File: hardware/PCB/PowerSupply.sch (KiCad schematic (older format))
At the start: 14 parts

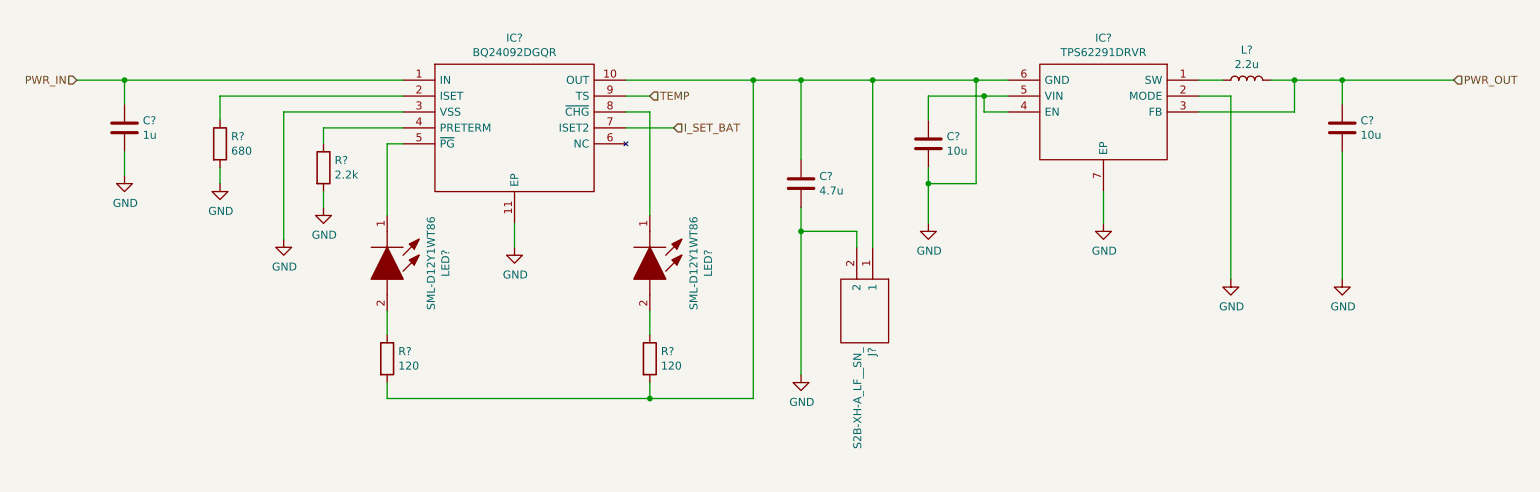
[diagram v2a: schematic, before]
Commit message: complete display circuit
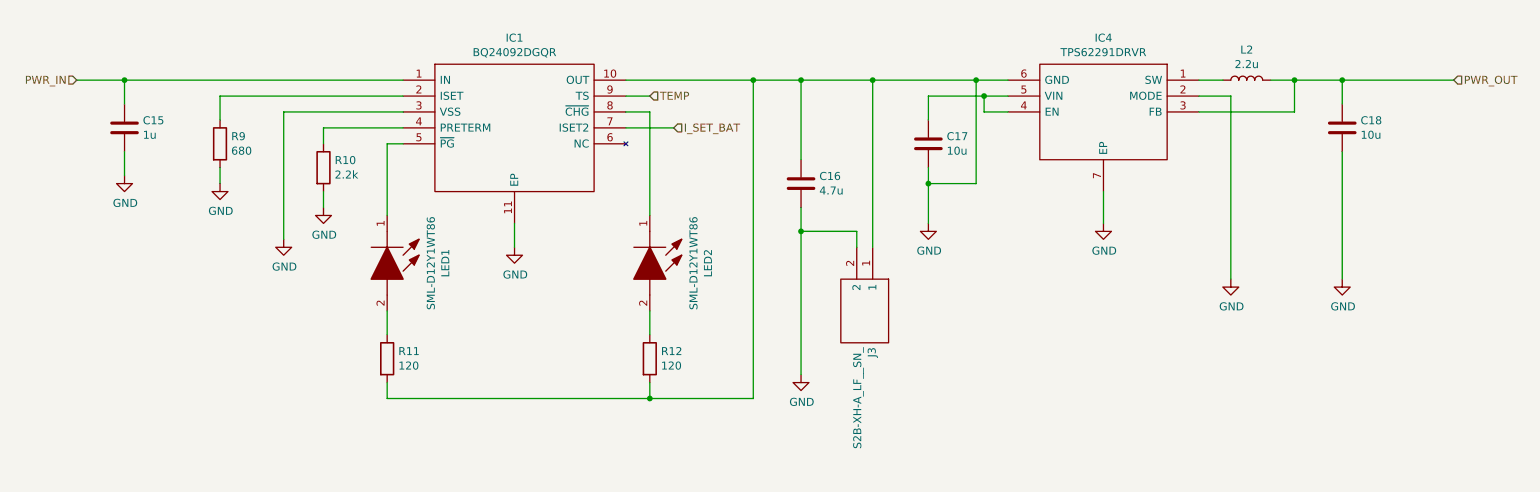
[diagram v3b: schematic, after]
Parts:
- gave numbers to parts that had none: 14
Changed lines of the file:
@@
 $EndDescr
 $Comp
-L ProjectLibrary:BQ24092DGQR IC?
+L ProjectLibrary:BQ24092DGQR IC1
 U 1 1 5FC01F89
 P 3250 1350
-F 0 "IC?" H 3950 1615 50  0000 C CNN
+F 0 "IC1" H 3950 1615 50  0000 C CNN
 F 1 "BQ24092DGQR" H 3950 1524 50  0000 C CNN
 F 2 "SOP50P490X110-11N" H 4500 1450 50  0001 L CNN
@@
 $EndComp
 $Comp
-L Device:C C?
+L Device:C C15
 U 1 1 5FC0418B
 P 1500 1650
-F 0 "C?" H 1615 1696 50  0000 L CNN
+F 0 "C15" H 1615 1696 50  0000 L CNN
 F 1 "1u" H 1615 1605 50  0000 L CNN
 F 2 "Capacitor_SMD:C_0603_1608Metric" H 1538 1500 50  0001 C CNN
@@
 Connection ~ 1500 1350
 $Comp
-L power:GND #PWR?
+L power:GND #PWR024
 U 1 1 5FC0983B
 P 2500 2350
-F 0 "#PWR?" H 2500 2100 50  0001 C CNN
+F 0 "#PWR024" H 2500 2100 50  0001 C CNN
 F 1 "GND" H 2505 2177 50  0000 C CNN
 F 2 "" H 2500 2350 50  0001 C CNN
@@
 	2500 1550 2500 2350
 $Comp
-L power:GND #PWR?
+L power:GND #PWR022
 U 1 1 5FC0A0A3
 P 1500 1950
-F 0 "#PWR?" H 1500 1700 50  0001 C CNN
+F 0 "#PWR022" H 1500 1700 50  0001 C CNN
 F 1 "GND" H 1505 1777 50  0000 C CNN
 F 2 "" H 1500 1950 50  0001 C CNN
@@
 $EndComp
 $Comp
-L Device:R R?
+L Device:R R9
 U 1 1 5FC0ABBE
 P 2100 1750
-F 0 "R?" H 2170 1796 50  0000 L CNN
+F 0 "R9" H 2170 1796 50  0000 L CNN
 F 1 "680" H 2170 1705 50  0000 L CNN
 F 2 "Resistor_SMD:R_0603_1608Metric" V 2030 1750 50  0001 C CNN
@@
 	2100 1900 2100 2000
 $Comp
-L power:GND #PWR?
+L power:GND #PWR023
 U 1 1 5FC0FEEE
 P 2100 2000
-F 0 "#PWR?" H 2100 1750 50  0001 C CNN
+F 0 "#PWR023" H 2100 1750 50  0001 C CNN
 F 1 "GND" H 2105 1827 50  0000 C CNN
 F 2 "" H 2100 2000 50  0001 C CNN
@@
 	2500 1550 3250 1550
 $Comp
-L Device:R R?
+L Device:R R10
 U 1 1 5FC11D4B
 P 2750 1900
-F 0 "R?" H 2820 1946 50  0000 L CNN
+F 0 "R10" H 2820 1946 50  0000 L CNN
 F 1 "2.2k" H 2820 1855 50  0000 L CNN
 F 2 "Resistor_SMD:R_0603_1608Metric" V 2680 1900 50  0001 C CNN
@@
 	2750 2050 2750 2150
 $Comp
-L power:GND #PWR?
+L power:GND #PWR025
 U 1 1 5FC12359
 P 2750 2150
-F 0 "#PWR?" H 2750 1900 50  0001 C CNN
+F 0 "#PWR025" H 2750 1900 50  0001 C CNN
 F 1 "GND" H 2755 1977 50  0000 C CNN
 F 2 "" H 2750 2150 50  0001 C CNN
@@
 $EndComp
 $Comp
-L power:GND #PWR?
+L power:GND #PWR026
 U 1 1 5FC12BAC
 P 3950 2400
-F 0 "#PWR?" H 3950 2150 50  0001 C CNN
+F 0 "#PWR026" H 3950 2150 50  0001 C CNN
 F 1 "GND" H 3955 2227 50  0000 C CNN
 F 2 "" H 3950 2400 50  0001 C CNN
@@
 PWR_OUT
 $Comp
-L ProjectLibrary:SML-D12Y1WT86 LED?
+L ProjectLibrary:SML-D12Y1WT86 LED1
 U 1 1 5FC1DAA7
 P 3150 2200
-F 0 "LED?" H 3450 2567 50  0000 C CNN
+F 0 "LED1" H 3450 2567 50  0000 C CNN
 F 1 "SML-D12Y1WT86" H 3450 2476 50  0000 C CNN
 F 2 "LEDC1608X55N" H 3650 2350 50  0001 L BNN
@@
 $EndComp
 $Comp
-L ProjectLibrary:SML-D12Y1WT86 LED?
+L ProjectLibrary:SML-D12Y1WT86 LED2
 U 1 1 5FC2377E
 P 4800 2200
-F 0 "LED?" H 5100 2567 50  0000 C CNN
+F 0 "LED2" H 5100 2567 50  0000 C CNN
 F 1 "SML-D12Y1WT86" H 5100 2476 50  0000 C CNN
 F 2 "LEDC1608X55N" H 5300 2350 50  0001 L BNN
@@
 	3150 2200 3150 1750
 $Comp
-L Device:R R?
+L Device:R R11
 U 1 1 5FC29AD8
 P 3150 3100
-F 0 "R?" H 3220 3146 50  0000 L CNN
+F 0 "R11" H 3220 3146 50  0000 L CNN
 F 1 "120" H 3220 3055 50  0000 L CNN
 F 2 "Resistor_SMD:R_0603_1608Metric" V 3080 3100 50  0001 C CNN
@@
 $EndComp
 $Comp
-L Device:R R?
+L Device:R R12
 U 1 1 5FC2A161
 P 4800 3100
-F 0 "R?" H 4870 3146 50  0000 L CNN
+F 0 "R12" H 4870 3146 50  0000 L CNN
 F 1 "120" H 4870 3055 50  0000 L CNN
 F 2 "Resistor_SMD:R_0603_1608Metric" V 4730 3100 50  0001 C CNN
@@
 	3950 2250 3950 2400
 $Comp
-L Device:C C?
+L Device:C C16
 U 1 1 5FC2DE09
 P 5750 2000
-F 0 "C?" H 5865 2046 50  0000 L CNN
+F 0 "C16" H 5865 2046 50  0000 L CNN
 F 1 "4.7u" H 5865 1955 50  0000 L CNN
 F 2 "Capacitor_SMD:C_0603_1608Metric" H 5788 1850 50  0001 C CNN
@@
 $EndComp
 $Comp
-L power:GND #PWR?
+L power:GND #PWR027
 U 1 1 5FC2E9CD
 P 5750 3200
-F 0 "#PWR?" H 5750 2950 50  0001 C CNN
+F 0 "#PWR027" H 5750 2950 50  0001 C CNN
 F 1 "GND" H 5755 3027 50  0000 C CNN
 F 2 "" H 5750 3200 50  0001 C CNN
@@
 	5750 1350 6200 1350
 $Comp
-L ProjectLibrary:S2B-XH-A_LF__SN_ J?
+L ProjectLibrary:S2B-XH-A_LF__SN_ J3
 U 1 1 5FC2F7E2
 P 6200 2400
-F 0 "J?" H 6828 2396 50  0000 L CNN
+F 0 "J3" H 6828 2396 50  0000 L CNN
 F 1 "S2B-XH-A_LF__SN_" H 6828 2305 50  0000 L CNN
 F 2 "SHDRRA2W80P0X250_1X2_740X1150X610P" H 6850 2500 50  0001 L CNN
@@
 $EndComp
 $Comp
-L ProjectLibrary:TPS62291DRVR IC?
+L ProjectLibrary:TPS62291DRVR IC4
 U 1 1 5FC09EEE
 P 8250 1350
-F 0 "IC?" H 8850 1615 50  0000 C CNN
+F 0 "IC4" H 8850 1615 50  0000 C CNN
 F 1 "TPS62291DRVR" H 8850 1524 50  0000 C CNN
 F 2 "SON65P200X200X80-7N" H 9300 1450 50  0001 L CNN
@@
 $EndComp
 $Comp
-L power:GND #PWR?
+L power:GND #PWR028
 U 1 1 5FC12B1D
 P 6550 2250
-F 0 "#PWR?" H 6550 2000 50  0001 C CNN
+F 0 "#PWR028" H 6550 2000 50  0001 C CNN
 F 1 "GND" H 6555 2077 50  0000 C CNN
 F 2 "" H 6550 2250 50  0001 C CNN
@@
 $EndComp
 $Comp
-L Device:C C?
+L Device:C C17
 U 1 1 5FC139FA
 P 6550 1750
-F 0 "C?" H 6665 1796 50  0000 L CNN
+F 0 "C17" H 6665 1796 50  0000 L CNN
 F 1 "10u" H 6665 1705 50  0000 L CNN
 F 2 "" H 6588 1600 50  0001 C CNN
@@
 	8250 1450 8450 1450
 $Comp
-L power:GND #PWR?
+L power:GND #PWR030
 U 1 1 5FC1A4A2
 P 8450 2600
-F 0 "#PWR?" H 8450 2350 50  0001 C CNN
+F 0 "#PWR030" H 8450 2350 50  0001 C CNN
 F 1 "GND" H 8455 2427 50  0000 C CNN
 F 2 "" H 8450 2600 50  0001 C CNN
@@
 $EndComp
 $Comp
-L power:GND #PWR?
+L power:GND #PWR029
 U 1 1 5FC1D2CA
 P 7650 2250
-F 0 "#PWR?" H 7650 2000 50  0001 C CNN
+F 0 "#PWR029" H 7650 2000 50  0001 C CNN
 F 1 "GND" H 7655 2077 50  0000 C CNN
 F 2 "" H 7650 2250 50  0001 C CNN
@@
 	7650 2050 7650 2250
 $Comp
-L Device:L L?
+L Device:L L2
 U 1 1 5FC1EB27
 P 8550 1350
-F 0 "L?" V 8740 1350 50  0000 C CNN
+F 0 "L2" V 8740 1350 50  0000 C CNN
 F 1 "2.2u" V 8649 1350 50  0000 C CNN
 F 2 "" H 8550 1350 50  0001 C CNN
@@
 	8250 1350 8400 1350
 $Comp
-L Device:C C?
+L Device:C C18
 U 1 1 5FC33F95
 P 9150 1650
-F 0 "C?" H 9265 1696 50  0000 L CNN
+F 0 "C18" H 9265 1696 50  0000 L CNN
 F 1 "10u" H 9265 1605 50  0000 L CNN
 F 2 "" H 9188 1500 50  0001 C CNN
@@
 	9150 1500 9150 1350
 $Comp
-L power:GND #PWR?
+L power:GND #PWR031
 U 1 1 5FC4D9AD
 P 9150 2600
-F 0 "#PWR?" H 9150 2350 50  0001 C CNN
+F 0 "#PWR031" H 9150 2350 50  0001 C CNN
 F 1 "GND" H 9155 2427 50  0000 C CNN
 F 2 "" H 9150 2600 50  0001 C CNN

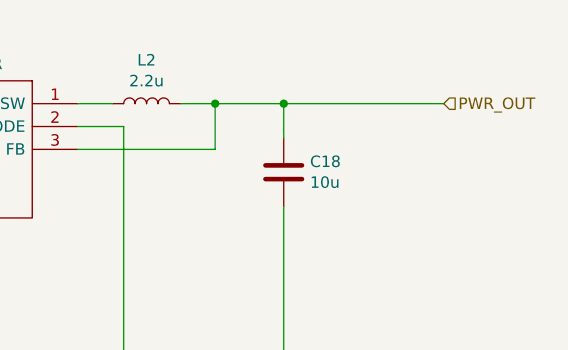
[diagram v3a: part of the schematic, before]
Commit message: change power out to 3V3
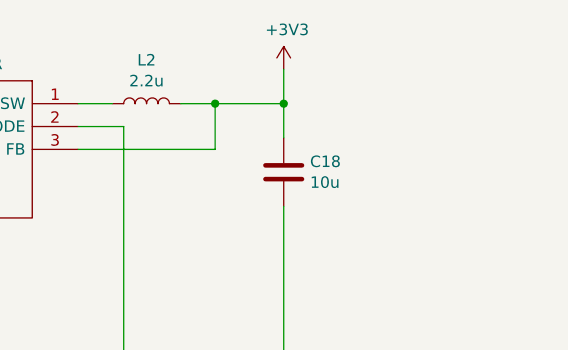
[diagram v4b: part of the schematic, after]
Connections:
- net PWR_OUT renamed +3V3
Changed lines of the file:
@@
 $Descr A4 11693 8268
 encoding utf-8
-Sheet 3 3
+Sheet 2 3
 Title ""
 Date ""
@@
 Wire Wire Line
 	4650 1550 4800 1550
-Text HLabel 9850 1350 2    50   Input ~ 0
-PWR_OUT
 $Comp
 L ProjectLibrary:SML-D12Y1WT86 LED1
@@
 	8850 1350 9150 1350
 Connection ~ 9150 1350
-Wire Wire Line
-	9150 1350 9850 1350
+$Comp
+L power:+3V3 #PWR?
+U 1 1 5FCF0BC9
+P 9150 1200
+F 0 "#PWR?" H 9150 1050 50  0001 C CNN
+F 1 "+3V3" H 9165 1373 50  0000 C CNN
+F 2 "" H 9150 1200 50  0001 C CNN
+F 3 "" H 9150 1200 50  0001 C CNN
+	1    9150 1200
+	1    0    0    -1
+$EndComp
+Wire Wire Line
+	9150 1200 9150 1350
 $EndSCHEMATC

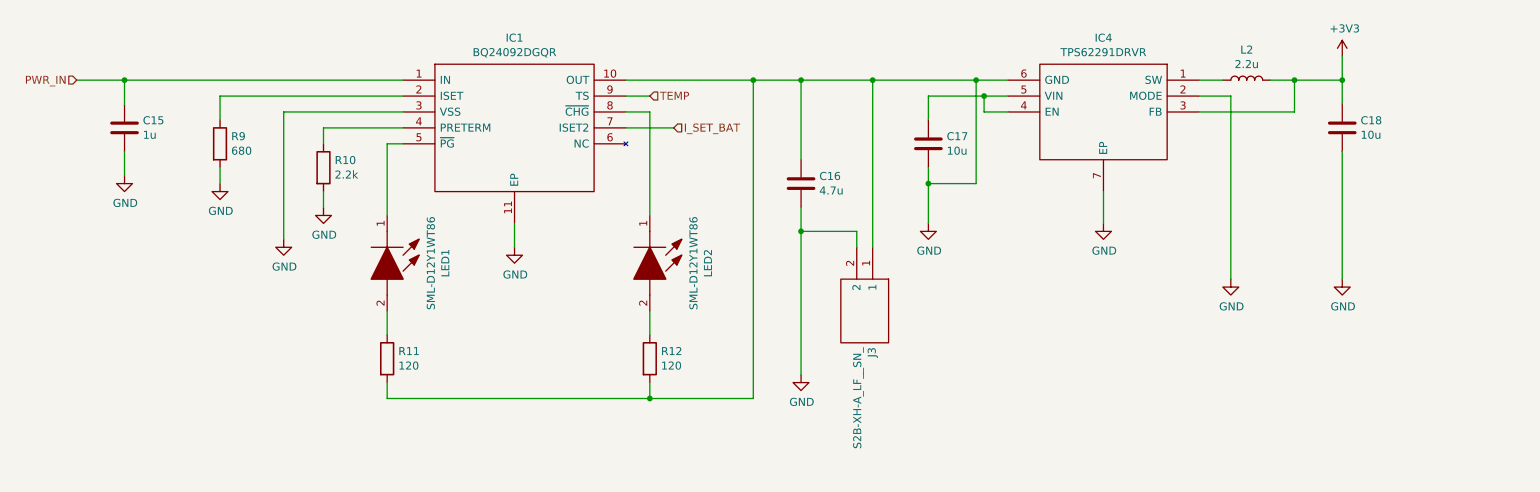
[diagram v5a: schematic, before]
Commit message: add 10k pull up
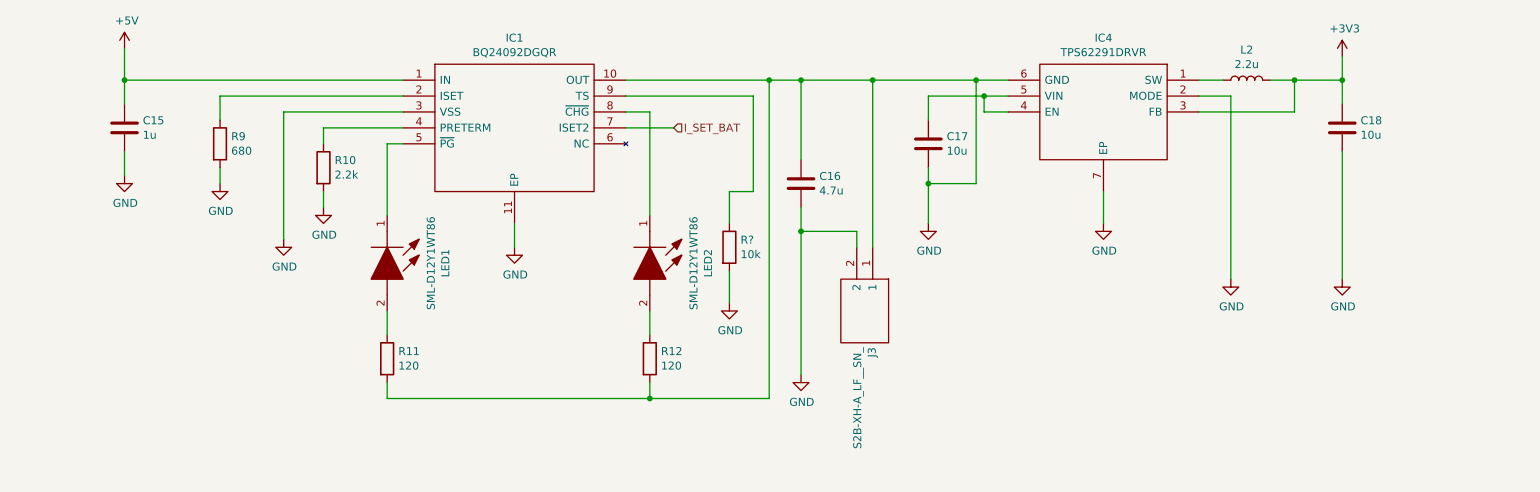
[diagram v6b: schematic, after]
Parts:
- added R?: 10k, Resistor_SMD:R_0603_1608Metric, symbol Device:R
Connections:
- net GND: now also R?.2
- net PWR_IN renamed +5V
- net TEMP: no longer names the net of IC1.9 (TS)
- net TEMP: now also R?.1
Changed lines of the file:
@@
 Wire Wire Line
 	1500 1350 1500 1500
-Text HLabel 1200 1350 0    50   Input ~ 0
-PWR_IN
-Wire Wire Line
-	1500 1350 1200 1350
 Connection ~ 1500 1350
 $Comp
@@
 Text HLabel 4950 1650 2    50   Input ~ 0
 I_SET_BAT
-Text HLabel 4800 1450 2    50   Input ~ 0
-TEMP
 Wire Wire Line
 	3250 1750 3150 1750
@@
 	0    1    1    0
 $EndComp
-Connection ~ 5450 1350
-Wire Wire Line
-	5450 1350 5750 1350
-Wire Wire Line
-	4650 1350 5450 1350
 Wire Wire Line
 	3150 2200 3150 1750
@@
 	4800 3350 4800 3250
 Wire Wire Line
-	4800 3350 5450 3350
-Wire Wire Line
-	5450 1350 5450 3350
+	5550 1350 5550 3350
 Connection ~ 4800 3350
 Wire Wire Line
@@
 $EndComp
 Wire Wire Line
-	4650 1450 4800 1450
-Wire Wire Line
 	4950 1650 4650 1650
 Wire Wire Line
@@
 Wire Wire Line
 	9150 1200 9150 1350
+$Comp
+L power:+5V #PWR?
+U 1 1 5FD7BBDC
+P 1500 1150
+F 0 "#PWR?" H 1500 1000 50  0001 C CNN
+F 1 "+5V" H 1515 1323 50  0000 C CNN
+F 2 "" H 1500 1150 50  0001 C CNN
+F 3 "" H 1500 1150 50  0001 C CNN
+	1    1500 1150
+	1    0    0    -1
+$EndComp
+Wire Wire Line
+	1500 1150 1500 1350
+$Comp
+L Device:R R?
+U 1 1 5FD81F10
+P 5300 2400
+F 0 "R?" H 5370 2446 50  0000 L CNN
+F 1 "10k" H 5370 2355 50  0000 L CNN
+F 2 "Resistor_SMD:R_0603_1608Metric" V 5230 2400 50  0001 C CNN
+F 3 "~" H 5300 2400 50  0001 C CNN
+	1    5300 2400
+	1    0    0    -1
+$EndComp
+Connection ~ 5550 1350
+Wire Wire Line
+	5550 1350 5750 1350
+Wire Wire Line
+	4650 1350 5550 1350
+Wire Wire Line
+	4800 3350 5550 3350
+Wire Wire Line
+	5450 1450 5450 2050
+Wire Wire Line
+	5450 2050 5300 2050
+Wire Wire Line
+	5300 2050 5300 2250
+Wire Wire Line
+	4650 1450 5450 1450
+$Comp
+L power:GND #PWR?
+U 1 1 5FD87B54
+P 5300 2750
+F 0 "#PWR?" H 5300 2500 50  0001 C CNN
+F 1 "GND" H 5305 2577 50  0000 C CNN
+F 2 "" H 5300 2750 50  0001 C CNN
+F 3 "" H 5300 2750 50  0001 C CNN
+	1    5300 2750
+	1    0    0    -1
+$EndComp
+Wire Wire Line
+	5300 2550 5300 2750
 $EndSCHEMATC

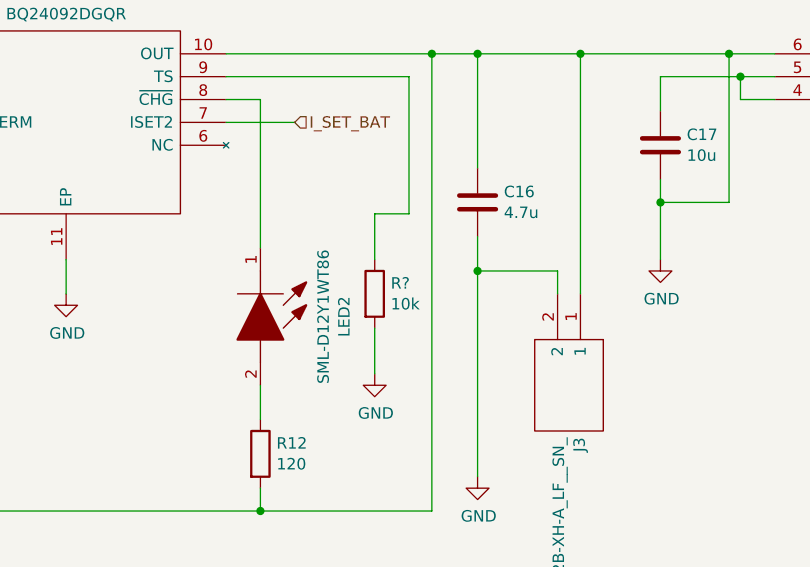
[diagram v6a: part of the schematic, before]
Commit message: add mechannical and usb ftdi sheet
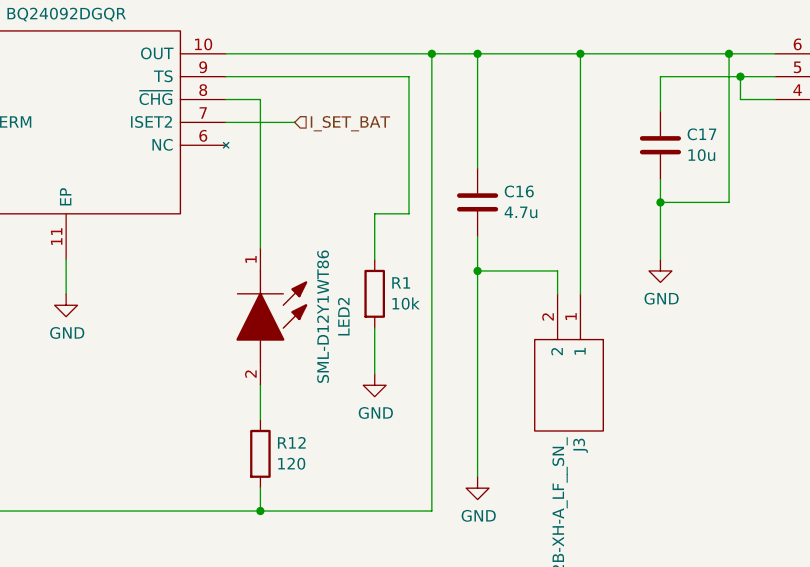
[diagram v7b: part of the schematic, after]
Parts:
- gave numbers to parts that had none: 1
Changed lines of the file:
@@
 $Descr A4 11693 8268
 encoding utf-8
-Sheet 2 5
+Sheet 2 7
 Title ""
 Date ""
@@
 Connection ~ 9150 1350
 $Comp
-L power:+3V3 #PWR?
+L power:+3V3 #PWR033
 U 1 1 5FCF0BC9
 P 9150 1200
-F 0 "#PWR?" H 9150 1050 50  0001 C CNN
+F 0 "#PWR033" H 9150 1050 50  0001 C CNN
 F 1 "+3V3" H 9165 1373 50  0000 C CNN
 F 2 "" H 9150 1200 50  0001 C CNN
@@
 	9150 1200 9150 1350
 $Comp
-L power:+5V #PWR?
+L power:+5V #PWR01
 U 1 1 5FD7BBDC
 P 1500 1150
-F 0 "#PWR?" H 1500 1000 50  0001 C CNN
+F 0 "#PWR01" H 1500 1000 50  0001 C CNN
 F 1 "+5V" H 1515 1323 50  0000 C CNN
 F 2 "" H 1500 1150 50  0001 C CNN
@@
 	1500 1150 1500 1350
 $Comp
-L Device:R R?
+L Device:R R1
 U 1 1 5FD81F10
 P 5300 2400
-F 0 "R?" H 5370 2446 50  0000 L CNN
+F 0 "R1" H 5370 2446 50  0000 L CNN
 F 1 "10k" H 5370 2355 50  0000 L CNN
 F 2 "Resistor_SMD:R_0603_1608Metric" V 5230 2400 50  0001 C CNN
@@
 	4650 1450 5450 1450
 $Comp
-L power:GND #PWR?
+L power:GND #PWR032
 U 1 1 5FD87B54
 P 5300 2750
-F 0 "#PWR?" H 5300 2500 50  0001 C CNN
+F 0 "#PWR032" H 5300 2500 50  0001 C CNN
 F 1 "GND" H 5305 2577 50  0000 C CNN
 F 2 "" H 5300 2750 50  0001 C CNN

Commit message: add ESP32 antenna
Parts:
- C17: footprint (none) -> Capacitor_SMD:C_0603_1608Metric
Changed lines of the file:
@@
 F 0 "C17" H 6665 1796 50  0000 L CNN
 F 1 "10u" H 6665 1705 50  0000 L CNN
-F 2 "" H 6588 1600 50  0001 C CNN
+F 2 "Capacitor_SMD:C_0603_1608Metric" H 6588 1600 50  0001 C CNN
 F 3 "~" H 6550 1750 50  0001 C CNN
 	1    6550 1750
